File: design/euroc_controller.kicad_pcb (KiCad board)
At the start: 4 copper layers, 35.1 x 77 mm, 87 parts, among them J1 xt30, J2 jst_sh 4, J4 jst_sh 4, J5 jst_sh 4, J6 SMA, J7 Screw_Terminal_01x06, J8 USB_C_Receptacle_USB2.0, J9 jst_sh 4, Q1 MMBT3904, U1 TPSM5601R5, U10 VN7050ASTR, U11 VN7050ASTR, U13 STM32U575CGTx, U2 USBLC6-2SC6, U3 LSM6DSO32, U4 MS5611-01BA, U5 TCAN332, U6 W25Q128JVS, U7 RFM69W, U8 L86, U9 VN7050ASTR, Y1 48MHz

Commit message: redo for aisler
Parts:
- added R27: 10k, Resistor_SMD:R_0603_1608Metric, B.Cu at (171.7, 75.0)
- C17: moved to B.Cu
- moved C17 2.54 mm to (183.1, 72.9)
- moved G*** 0.36 mm to (174.0, 49.3)
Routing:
- net /BOOT0: track 23.1 -> 33.9 mm
- net Earth: track 105.0 -> 109.1 mm
- net +3V3: track 58.1 -> 57.6 mm

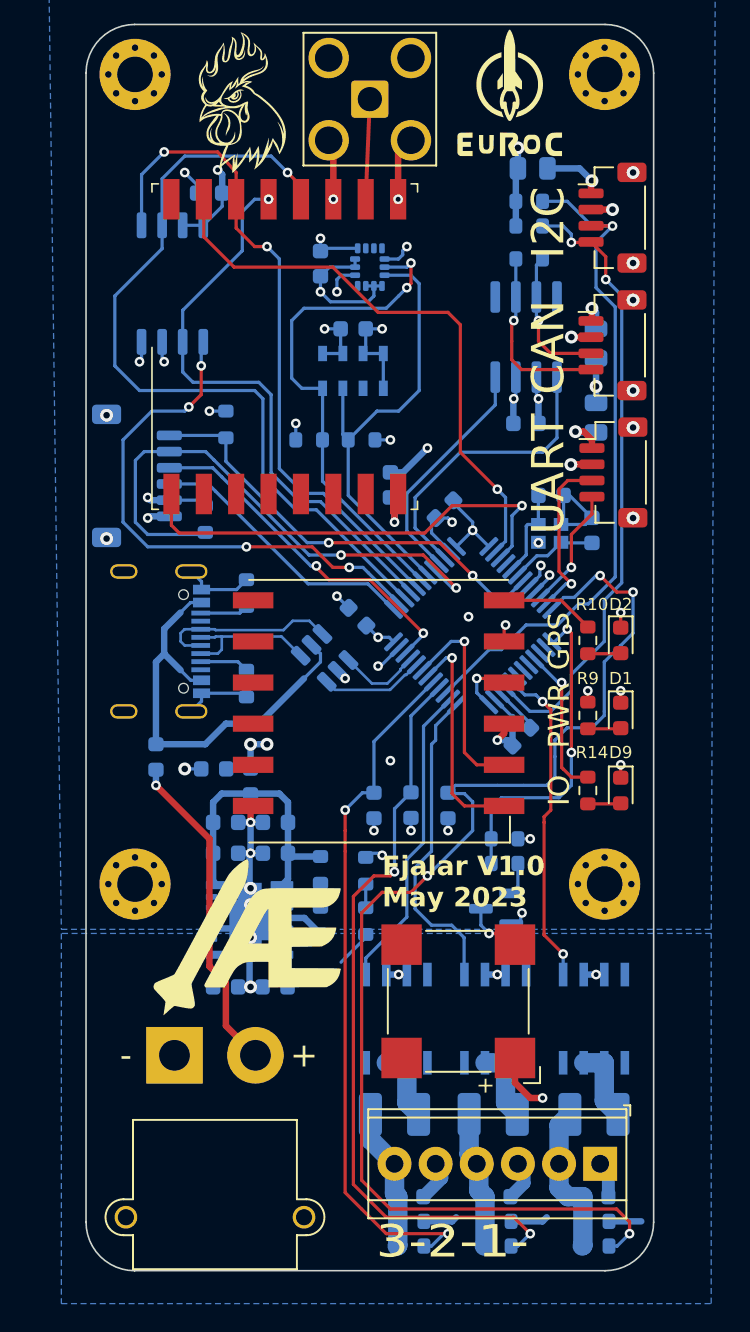
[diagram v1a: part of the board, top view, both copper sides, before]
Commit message: PCB 1.1 old regulator
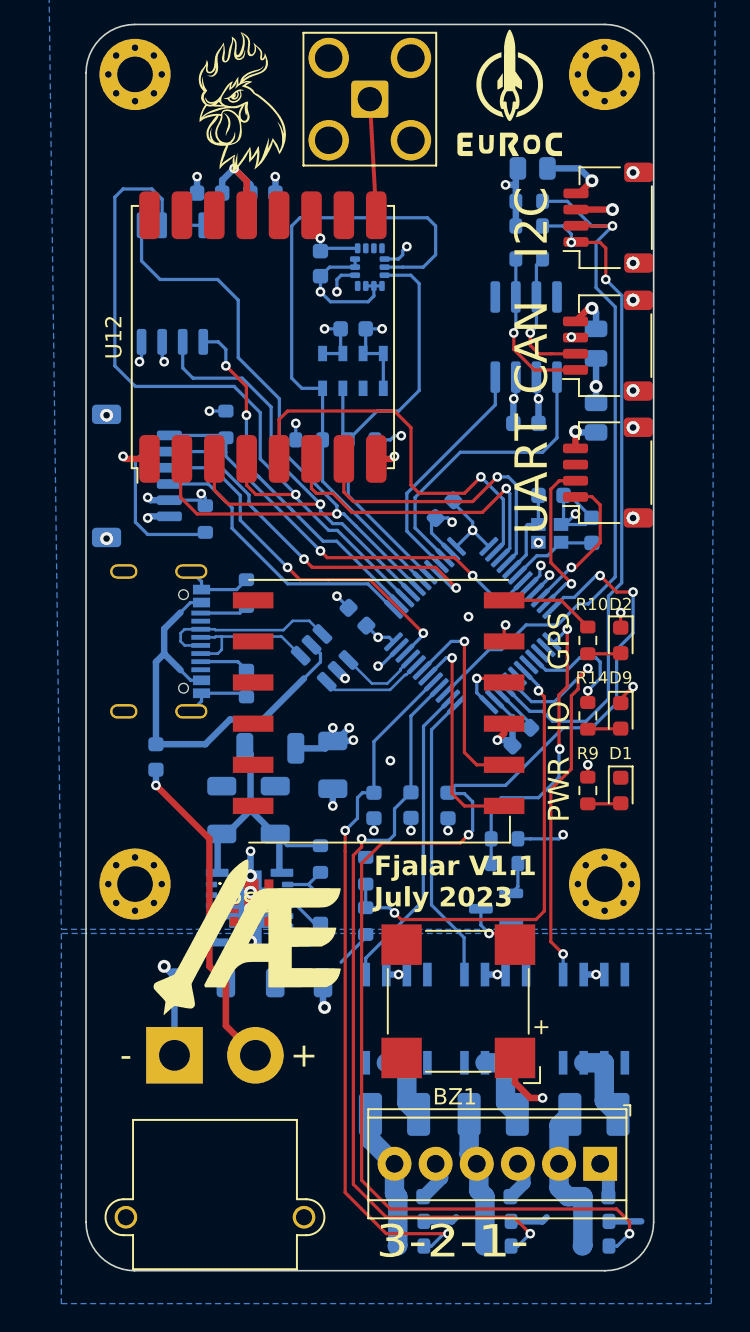
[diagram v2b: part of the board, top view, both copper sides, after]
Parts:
- removed C5, C8: 47u, Capacitor_SMD:C_0603_1608Metric
- removed U7: RFM69W, RF_Module:HOPERF_RFM69HW
- added PS1: TPSM82901SISR, lib:TPSM82901SISR, F.Cu at (174.6, 98.7)
- added U12: RFM98W-433S2, RF_Module:HOPERF_RFM9XW_SMD, F.Cu at (175.3, 63.8)
- C1, C15, C2, C3, C4: footprint Capacitor_SMD:C_0603_1608Metric -> Capacitor_SMD:C_1206_3216Metric
- C13, C14: value 22p -> 14p
- J2, J4, J5: footprint Connector_JST:JST_SH_BM04B-SRSS-TB_1x04-1MP_P1.00mm_Vertical -> Connector_JST:JST_SH_SM04B-SRSS-TB_1x04-1MP_P1.00mm_Horizontal
- L1: value L_Small -> 1u5; footprint Inductor_SMD:L_0603_1608Metric -> Inductor_SMD:L_1206_3216Metric
- R10, R14, R19, R9: value 1k -> 470
- R23, R24, R26: value 100 -> 120
- moved C17 19.7 mm to (175.3, 54.9), turned to 0 degrees
- moved C15 7.36 mm to (179.6, 90.2), turned to -90 degrees
- moved D1 4.64 mm to (197.4, 91.8)
- moved R9 4.64 mm to (195.3, 91.8)
- moved D9 4.61 mm to (197.4, 87.1)
- moved R14 4.61 mm to (195.3, 87.1)
- moved C3 3.15 mm to (176.0, 93.0), turned to 90 degrees
- moved C4 2.68 mm to (172.7, 93.0), turned to 90 degrees
- moved L1 2.38 mm to (175.7, 89.2), turned to 0 degrees
- moved C2 1.51 mm to (177.5, 103.6), turned to 0 degrees
- moved C1 1.48 mm to (171.5, 103.6), turned to 180 degrees
- moved U1 0.76 mm to (174.4, 99.0)
- moved R7 0.67 mm to (178.8, 96.0)
- moved R8 0.67 mm to (178.8, 99.1)
- moved J5 0.34 mm to (196.6, 72.1), turned to 90 degrees
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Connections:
- J2 pad 1: Net-(J2-Pin_1) -> /EXT_SCL
- J2 pad 2: Earth -> /EXT_SDA
- J2 pad 3: /EXT_SDA -> Earth
- J2 pad 4: /EXT_SCL -> Net-(J2-Pin_4)
- J4 pad 1: Net-(J4-Pin_1) -> /CAN_L
- J4 pad 2: Earth -> /CAN_H
- J4 pad 3: /CAN_H -> Earth
- J4 pad 4: /CAN_L -> Net-(J4-Pin_4)
- J5 pad 1: Net-(J5-Pin_1) -> /EXT_TX
- J5 pad 2: Earth -> /EXT_RX
- J5 pad 3: /EXT_RX -> Earth
- J5 pad 4: /EXT_TX -> Net-(J5-Pin_4)
- R23 pad 1: Net-(J5-Pin_1) -> Net-(J5-Pin_4)
- R24 pad 1: Net-(J2-Pin_1) -> Net-(J2-Pin_4)
- R26 pad 1: Net-(J4-Pin_1) -> Net-(J4-Pin_4)
- U13 pad 18: unconnected-(U13-PB0-Pad18) -> /VBAT_SENSE
- U13 pad 4: unconnected-(U13-PC15-Pad4) -> /LORA_DIO
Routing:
- net /VBAT_SENSE: track 1.46 -> 28.4 mm, vias 0 -> 2
- net /LORA_DIO: track 0.00 -> 18.9 mm, vias 0 -> 1
- net /FLASH_CS: track 33.5 -> 22.2 mm, vias 4 -> 2
- net /LORA_CS: track 35.9 -> 25.2 mm
- net /SCL: track 31.5 -> 40.6 mm, vias 2 -> 0
- net Earth: track 109.1 -> 100.1 mm, vias 50 -> 48
- net /LORA_RESET: track 28.3 -> 19.7 mm
- net /PYRO3_EN: track 20.1 -> 26.2 mm
- net +3V3: track 57.6 -> 62.1 mm
- net Net-(J2-Pin_4): track 0.00 -> 4.37 mm, vias 0 -> 1
- net /SCK: track 50.2 -> 46.0 mm
- net Net-(J2-Pin_1): track 3.87 -> 0.00 mm, vias 1 -> 0
- net /MISO: track 35.9 -> 32.3 mm
- net Net-(J5-Pin_1): track 3.02 -> 0.00 mm, vias 1 -> 0
- net Net-(J4-Pin_4): track 0.00 -> 2.73 mm, vias 0 -> 1
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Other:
- board text added: "Fjalar V1.1 July 2023"
- board text removed: "Fjalar V1.0 May 2023"
- board text removed: "ROUTE LORA"
- board text removed: "ROUTE USB"

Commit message: PCB v1.1
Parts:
- removed C15: 47u, Capacitor_SMD:C_1206_3216Metric
- removed PS1: TPSM82901SISR, lib:TPSM82901SISR
- added C5: 10u, Capacitor_SMD:C_1206_3216Metric, B.Cu at (177.6, 104.1)
- added R28: 10k, Resistor_SMD:R_0603_1608Metric, B.Cu at (185.6, 97.0)
- added R29: 10k, Resistor_SMD:R_0603_1608Metric, B.Cu at (185.6, 98.8)
- added R30: 10k, Resistor_SMD:R_0603_1608Metric, B.Cu at (185.6, 100.6)
- C1: value 4u7 -> N/A; footprint Capacitor_SMD:C_1206_3216Metric -> Capacitor_SMD:C_0603_1608Metric
- C2: value 4u7 -> 10u
- C3, C4: value 47u -> 22u; footprint Capacitor_SMD:C_1206_3216Metric -> Capacitor_SMD:C_0805_2012Metric
- D10, D3, D4, D7: footprint Diode_SMD:D_0603_1608Metric -> Diode_SMD:D_SOD-323_HandSoldering
- L1: value 1u5 -> 1u; footprint Inductor_SMD:L_1206_3216Metric -> Inductor_SMD:L_0805_2012Metric
- R7: value 10k -> N/A
- R8: value 4.3k -> 26k1; footprint Resistor_SMD:R_0603_1608Metric -> Capacitor_SMD:C_0603_1608Metric
- U1: value TPSM5601R5 -> TPSM82901SISR; footprint Package_DFN_QFN:Texas_B3QFN-14-1EP_5x5.5mm_P0.65mm -> lib:uSIP11_SIS_TEX
- moved R8 5.55 mm to (174.0, 101.9), turned to 90 degrees
- moved R7 5.53 mm to (173.5, 94.3), turned to 180 degrees
- moved C3 4.63 mm to (178.6, 96.8), turned to -90 degrees
- moved L1 2.10 mm to (176.1, 91.2), turned to 90 degrees
- moved C2 2.10 mm to (177.6, 101.5), turned to 180 degrees
- moved C4 1.99 mm to (173.6, 91.2), turned to -90 degrees
- moved C1 1.90 mm to (172.2, 101.9), turned to 90 degrees
- moved U1 1.41 mm to (175.0, 97.7), turned to 90 degrees
- moved D3 1.20 mm to (181.1, 92.1)
- moved D4 0.79 mm to (183.9, 92.1)
- moved D7 0.63 mm to (186.7, 92.1)
- moved D10 0.48 mm to (168.7, 90.2)
- moved J2 0.35 mm to (196.2, 56.4)
- moved J4 0.32 mm to (196.2, 64.3)
- moved J5 0.32 mm to (196.2, 72.1)
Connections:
- C1 pad 1: VCC -> Earth
- C1 pad 2: Earth -> Net-(U1-SS/TR)
- C2 pad 1: VCC -> Earth
- C2 pad 2: Earth -> VCC
- C3 pad 1: Net-(C3-Pad1) -> /3v3_raw
- C4 pad 1: Net-(C3-Pad1) -> +3V3
- L1 pad 1: Net-(C3-Pad1) -> /3v3_raw
- R7 pad 1: Net-(C3-Pad1) -> Net-(U1-FB/VSET)
- R7 pad 2: Net-(U1-FB) -> Earth
- R8 pad 1: Net-(U1-FB) -> Earth
- R8 pad 2: Earth -> Net-(U1-MODE/S-CONF)
- U1 pad 10: Earth -> /3v3_raw
- U1 pad 3: Earth -> VCC
- U1 pad 4: unconnected-(U1-DNC-Pad4) -> Net-(U1-MODE/S-CONF)
- U1 pad 5: unconnected-(U1-DNC-Pad5) -> Net-(U1-SS/TR)
- U1 pad 7: Net-(C3-Pad1) -> Net-(U1-FB/VSET)
- U1 pad 8: Net-(C3-Pad1) -> unconnected-(U1-SW/NC-Pad8)
- U1 pad 9: Net-(U1-FB) -> /3v3_raw
- U12 pad 14: unconnected-(U12-DIO0-Pad14) -> /LORA_DIO
- U12 pad 7: /LORA_DIO -> unconnected-(U12-DIO5-Pad7)
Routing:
- net /LORA_DIO: track 18.9 -> 51.0 mm, vias 1 -> 3
- net Net-(C3-Pad1): track 17.0 -> 0.00 mm
- net /PYRO3_EN: track 26.2 -> 38.6 mm
- net VCC: track 30.0 -> 19.3 mm, vias 1 -> 2
- net /3v3_raw: track 0.00 -> 7.73 mm
- net Earth: track 100.1 -> 96.1 mm, vias 48 -> 45
- net Net-(U1-FB): track 3.43 -> 0.00 mm
- net Net-(U1-SS/TR): track 0.00 -> 3.02 mm
- net Net-(U1-MODE/S-CONF): track 0.00 -> 2.55 mm
- net /PYRO1_EN: track 19.2 -> 21.7 mm
- net Net-(U1-FB/VSET): track 0.00 -> 2.40 mm
- net /PYRO2_EN: track 18.1 -> 20.0 mm
- net /EXT_SCL: track 41.1 -> 42.7 mm
- net /SW_DIO: track 22.5 -> 23.9 mm
- net /PYRO1_SENSE: track 43.2 -> 44.3 mm
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- added copper zone on B.Cu, net /3v3_raw

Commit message: v1.2
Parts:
- removed the G*** at (190.5, 48.8)
- removed J4, J5: jst_sh 4, Connector_JST:JST_SH_SM04B-SRSS-TB_1x04-1MP_P1.00mm_Horizontal
- removed L1: 1u, Inductor_SMD:L_0805_2012Metric
- removed R21, R22: 5k1, Resistor_SMD:R_0603_1608Metric
- removed R23, R24, R26: 120, Resistor_SMD:R_0805_2012Metric
- removed R7: N/A, Resistor_SMD:R_0603_1608Metric
- removed R8: 26k1, Capacitor_SMD:C_0603_1608Metric
- removed U1: TPSM82901SISR, lib:uSIP11_SIS_TEX
- added C15: 1u, Capacitor_SMD:C_0603_1608Metric, B.Cu at (170.8, 92.9)
- added C18: 10u, Capacitor_SMD:C_0603_1608Metric, B.Cu at (176.0, 91.3)
- added C19: 10u, Capacitor_SMD:C_0603_1608Metric, B.Cu at (176.0, 92.8)
- added C20: 220n, Capacitor_SMD:C_0603_1608Metric, B.Cu at (173.7, 59.2)
- added C21: 100n, Capacitor_SMD:C_0603_1608Metric, B.Cu at (175.8, 56.8)
- added C8: 1u, Capacitor_SMD:C_0603_1608Metric, B.Cu at (171.8, 95.6)
- added FB2: BLM18KG102SN1D, Inductor_SMD:L_0805_2012Metric_Pad1.15x1.40mm_HandSolder, B.Cu at (178.0, 102.6)
- added FB4: BLM18KG102SN1D, Inductor_SMD:L_0805_2012Metric_Pad1.15x1.40mm_HandSolder, B.Cu at (172.6, 92.9)
- added G***: LOGO, LOGO, F.Cu at (196.1, 104.7)
- added G***: LOGO, LOGO, F.Cu at (189.9, 49.7)
- added IC1: LMR50410Y3, Package_TO_SOT_SMD:SOT-23-6_Handsoldering, B.Cu at (177.0, 96.1)
- added J3: jst gh 4, Connector_JST:JST_GH_SM04B-GHS-TB_1x04-1MP_P1.25mm_Horizontal, F.Cu at (196.4, 56.5)
- added JP1: SolderJumper_2_Open, Jumper:SolderJumper-2_P1.3mm_Open_TrianglePad1.0x1.5mm, B.Cu at (190.3, 51.8)
- added JP2: SolderJumper_2_Open, Jumper:SolderJumper-2_P1.3mm_Open_TrianglePad1.0x1.5mm, B.Cu at (190.3, 54.5)
- added L2: 4.7u, Inductor_SMD_Wurth:L_Wurth_WE-LQSH-3012, B.Cu at (173.2, 98.6)
- added SW1: SW_SPST, Button_Switch_SMD:SW_SPST_B3U-1000P, B.Cu at (179.3, 88.0)
- added U7: LIS2MDL, Package_LGA:LGA-12_2x2mm_P0.5mm, B.Cu at (176.0, 59.5)
- C1: value N/A -> 1u
- C2: value 10u -> 1u; footprint Capacitor_SMD:C_1206_3216Metric -> Capacitor_SMD:C_0603_1608Metric
- C3: value 22u -> 1u; footprint Capacitor_SMD:C_0805_2012Metric -> Capacitor_SMD:C_0603_1608Metric
- C4: value 22u -> 100n; footprint Capacitor_SMD:C_0805_2012Metric -> Capacitor_SMD:C_0603_1608Metric
- C5: value 10u -> 100n; footprint Capacitor_SMD:C_1206_3216Metric -> Capacitor_SMD:C_0603_1608Metric
- J2: value jst_sh 4 -> jst gh 6; footprint Connector_JST:JST_SH_SM04B-SRSS-TB_1x04-1MP_P1.00mm_Horizontal -> Connector_JST:JST_GH_SM06B-GHS-TB_1x06-1MP_P1.25mm_Horizontal
- J9: value jst_sh 4 -> jst_sh 6
- R11, R12, R17, R3, R4, R5: value 47k -> 3k
- U8: value L86 -> LC86
- moved C4 13.3 mm to (175.0, 104.4), turned to 0 degrees
- moved J2 11.0 mm to (196.3, 67.4)
- moved C5 9.32 mm to (174.4, 95.4), turned to -90 degrees
- moved C1 6.27 mm to (178.0, 104.4), turned to 0 degrees
- moved C3 4.09 mm to (178.0, 100.9), turned to 180 degrees
- moved R25 2.84 mm to (189.2, 57.5), turned to -90 degrees
- moved C7 2.27 mm to (171.8, 52.6)
- moved C17 2.26 mm to (175.2, 52.6)
- moved C2 2.19 mm to (178.0, 99.4)
- moved C16 1.61 mm to (190.0, 68.5)
- moved U5 1.52 mm to (190.0, 63.7)
- moved C13 0.36 mm to (192.7, 73.5)
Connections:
- C1 pad 2: Net-(U1-SS/TR) -> VCC
- C2 pad 2: VCC -> /VCC_FILT
- C3 pad 1: /3v3_raw -> Earth
- C3 pad 2: Earth -> /VCC_FILT
- C4 pad 1: +3V3 -> Earth
- C4 pad 2: Earth -> /VCC_FILT
- C5 pad 1: VCC -> /CB
- C5 pad 2: Earth -> /SW
- J2 pad 1: /EXT_SCL -> +3V3
- J2 pad 2: /EXT_SDA -> /EXT_RX
- J2 pad 3: Earth -> /EXT_TX
- J2 pad 4: Net-(J2-Pin_4) -> /EXT_IO0
- R25 pad 1: /CAN_H -> Net-(JP2-A)
- U12 pad 2: /MOSI -> /MISO
- U12 pad 3: /MISO -> /MOSI
- U13 pad 14: unconnected-(U13-PA4-Pad14) -> /EXT_IO1
- U13 pad 15: unconnected-(U13-PA5-Pad15) -> /EXT_IO0
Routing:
- net VCC: track 19.3 -> 83.4 mm
- net /EXT_SDA: track 43.3 -> 0.00 mm, vias 1 -> 0
- net /EXT_SCL: track 42.7 -> 0.00 mm, vias 2 -> 0
- net /EXT_IO1: track 0.00 -> 24.1 mm, vias 0 -> 1
- net /EXT_IO0: track 0.00 -> 23.5 mm, vias 0 -> 1
- net /OUT_RAW: track 0.00 -> 17.3 mm
- net /SDA: track 28.3 -> 41.7 mm, vias 0 -> 2
- net /BOOT0: track 34.2 -> 46.1 mm, vias 2 -> 3
- net Net-(J3-Pin_1): track 0.00 -> 11.4 mm, vias 0 -> 1
- net /VCC_FILT: track 0.00 -> 8.50 mm
- net +3V3: track 61.0 -> 68.8 mm, vias 22 -> 24
- net /3v3_raw: track 7.73 -> 0.00 mm
- net /EXT_RX: track 10.7 -> 16.7 mm
- net /EXT_TX: track 9.50 -> 15.0 mm
- net /SW: track 0.00 -> 4.65 mm
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- removed copper zone on B.Cu, net /3v3_raw
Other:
- board text added: "Fjalar V1.2 Oct 2025"
- board text added: "TERM"
- board text removed: "Fjalar V1.1 July 2023"
- board text removed: "I2C"
